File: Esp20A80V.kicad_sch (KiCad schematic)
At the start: 19 parts, among them J1 dcdc, J4 I2C/Uart, Q1 SI2305, SW1 3x button, U1 spi tft with touch (+ sd card), U3 20A 80V dcdc, U4 Wemos S2 Mini

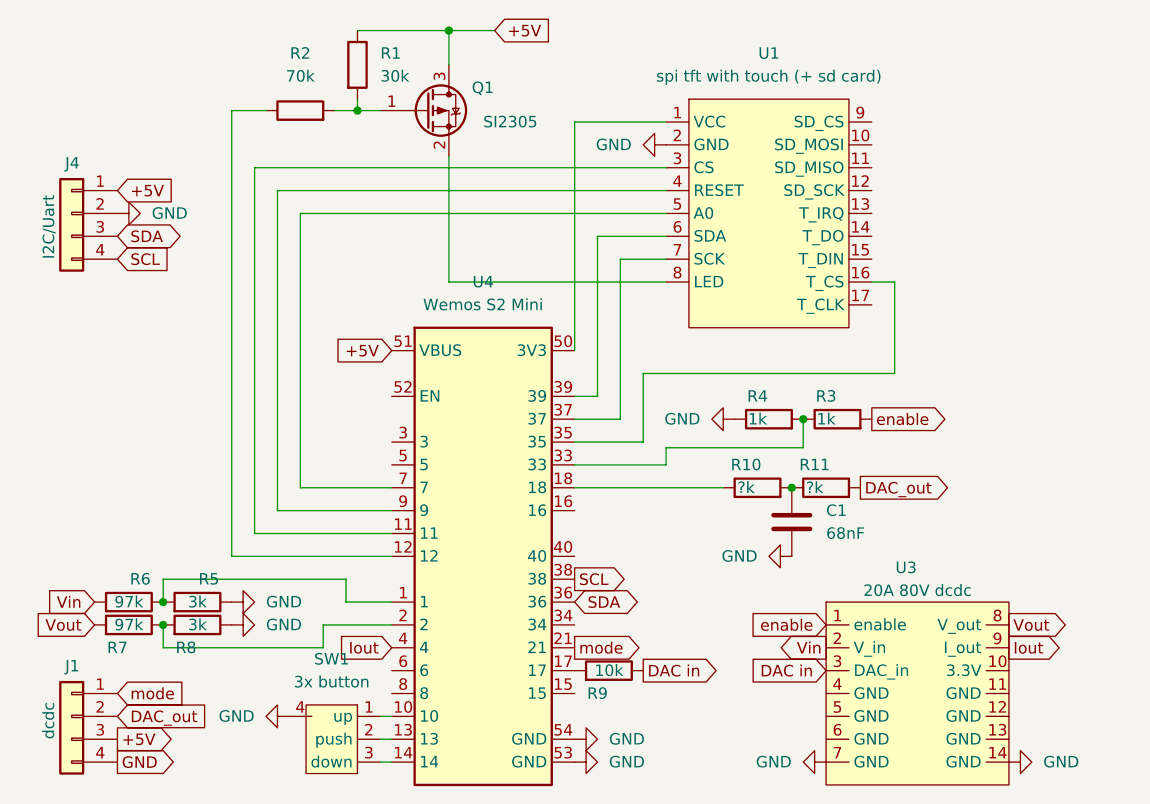
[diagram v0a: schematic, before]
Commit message: footsprints verified and sd card added
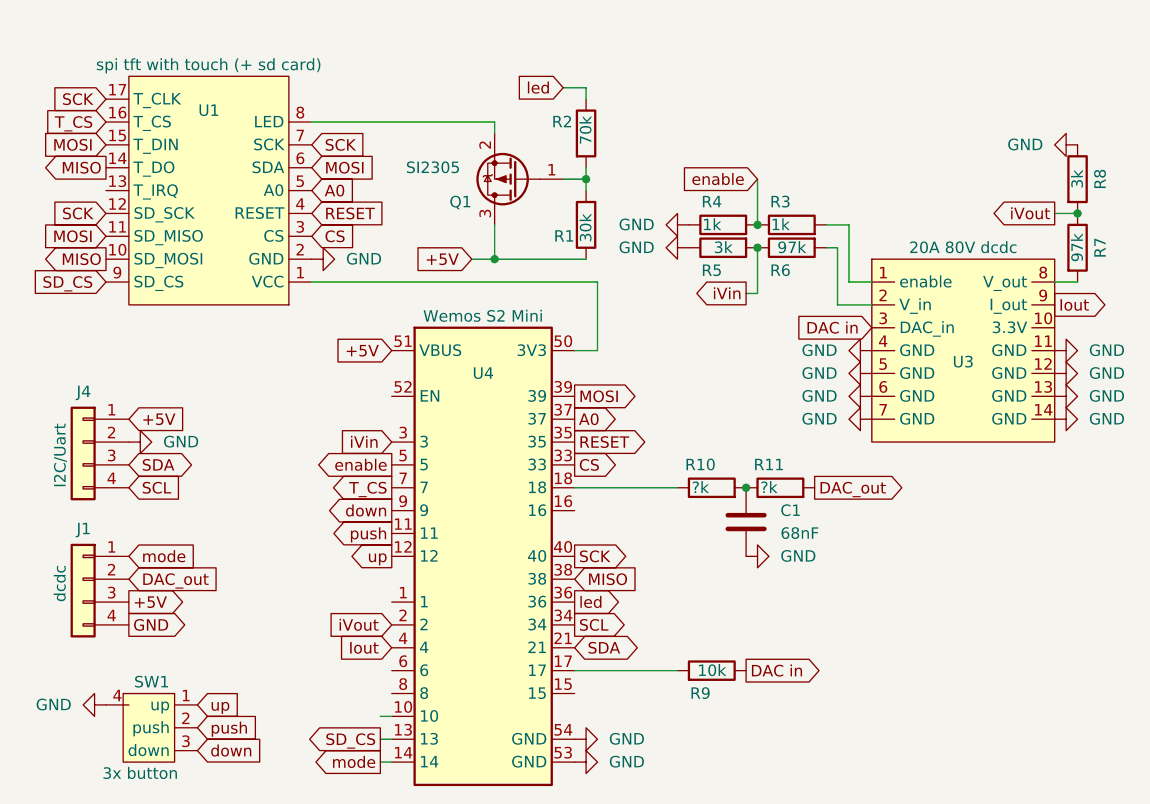
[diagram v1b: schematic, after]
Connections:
- net GND: now also U3.11 (GND), U3.12 (GND), U3.13 (GND), U3.4 (GND), U3.5 (GND), U3.6 (GND)
- net SCL: now also U4.34; no longer U4.38
- net SDA: now also U4.21; no longer U4.36
- net enable: now also R3.1, R4.2, U4.5; no longer R3.2, U3.1 (enable)
- net mode: now also U4.14; no longer U4.21
- net MISO: now reaches U1.10 (SD_MOSI)
- net MISO: now also U1.14 (T_DO), U4.38
- net MOSI: now reaches U1.11 (SD_MISO)
- net MOSI: now also U1.15 (T_DIN), U1.6 (SDA), U4.39
- net SCK: now reaches U1.12 (SD_SCK)
- net SCK: now also U1.17 (T_CLK), U1.7 (SCK), U4.40
- net RESET: now reaches U4.35
- net RESET: now also U1.4 (RESET); no longer U1.16 (T_CS)
- net CS: now reaches U1.3 (CS)
- net CS: now also U4.33; no longer U4.11
- net down: now reaches U4.9
- net down: now also SW1.3 (down); no longer U1.4 (RESET)
- net A0: now reaches U1.5 (A0)
- net A0: now also U4.37; no longer U4.7
- net SD_CS: now reaches U1.9 (SD_CS)
- net SD_CS: now also U4.13
- net iVout: now reaches R7.1, R8.2, U4.2
- net iVin: now reaches R5.2, R6.1
- net iVin: now also U4.3; no longer U4.1
- net at U4.10: no longer SW1.1 (up)
- net push: now reaches SW1.2 (push)
- net push: now also U4.11; no longer U4.13
- net led: now reaches R2.1
- net led: now also U4.36; no longer U4.12
- net Vin: no longer names the net of R6.2, U3.2 (V_in)
- net Vout: no longer names the net of R7.2, U3.8 (V_out)
- new net: R3.2, U3.1 (enable)
- new net T_CS: U1.16 (T_CS), U4.7
- new net up: SW1.1 (up), U4.12
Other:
- moved on the sheet: C1, J1, J4, Q1, R1, R10, R11, R2, R3, R4, R5, R6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

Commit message: jst ph2.0 instead of dupont female
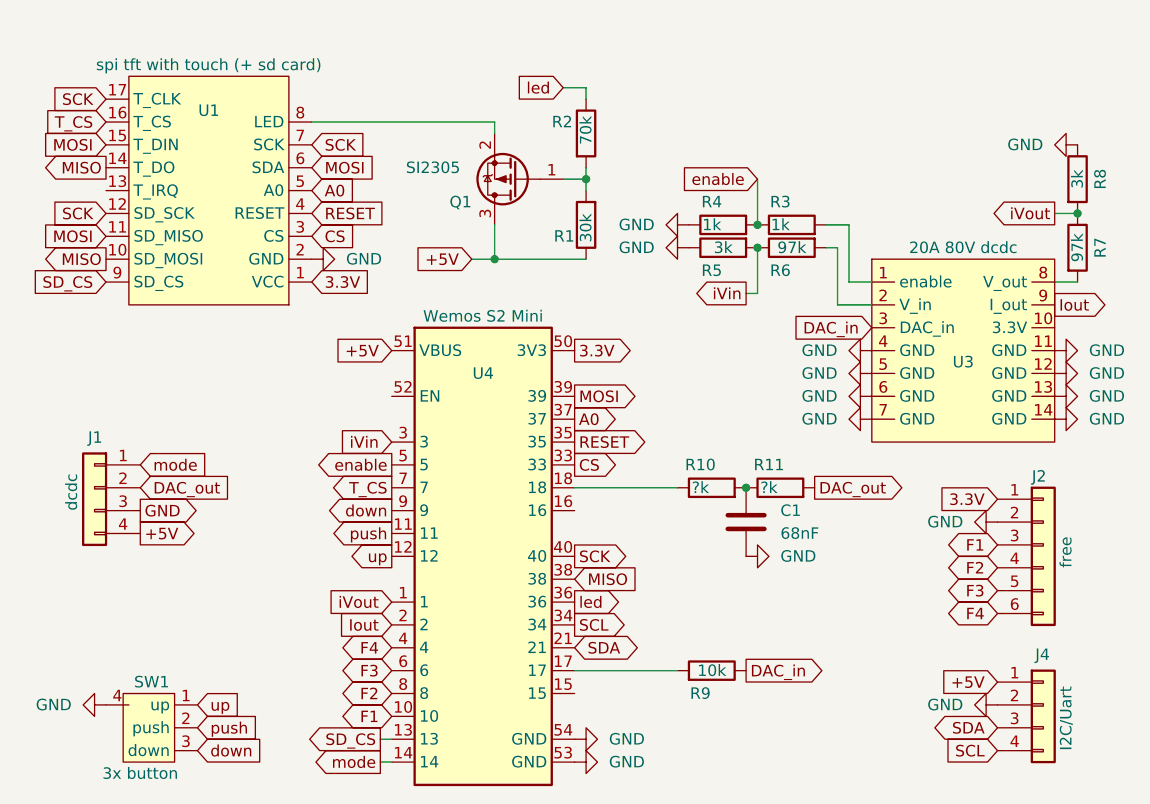
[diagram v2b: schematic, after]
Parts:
- added J2: free, Connector_PinHeader_2.54mm:PinHeader_1x06_P2.54mm_Horizontal, symbol Connector_Generic:Conn_01x06
- J1: footprint Connector_PinHeader_2.54mm:PinHeader_1x04_P2.54mm_Vertical -> Connector_JST:JST_PH_B4B-PH-K_1x04_P2.00mm_Vertical
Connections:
- net +5V: now also J1.4 (Pin_4); no longer J1.3 (Pin_3)
- net GND: now also J1.3 (Pin_3), J2.2 (Pin_2); no longer J1.4 (Pin_4)
- net Iout: now also U4.2; no longer U4.4
- net iVout: now also U4.1; no longer U4.2
- net 3.3V: now reaches U1.1 (VCC), U4.50 (3V3)
- net 3.3V: now also J2.1 (Pin_1)
- net F1: now reaches U4.10
- net F1: now also J2.3 (Pin_3)
- net F3: now reaches U4.6
- net F3: now also J2.5 (Pin_5)
- net F2: now reaches U4.8
- net F2: now also J2.4 (Pin_4)
- net DAC in renamed DAC_in
- new net F4: J2.6 (Pin_6), U4.4
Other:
- moved on the sheet: J1, J4

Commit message: update
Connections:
- net DAC_out: now also J1.1 (Pin_1); no longer J1.2 (Pin_2)
- net mode: now also J1.2 (Pin_2); no longer J1.1 (Pin_1)
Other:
- moved on the sheet: J1, SW1
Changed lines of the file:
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@@
     )
   )
-  (global_label "push" (shape input) (at 107.95 118.11 0) (fields_autoplaced)
-    (effects (font (size 1.27 1.27)) (justify left))
-    (property "Intersheetrefs" "${INTERSHEET_REFS}" (at 115.4103 118.11 0)
+  (global_label "push" (shape input) (at 107.95 96.52 0) (fields_autoplaced)
+    (effects (font (size 1.27 1.27)) (justify left))
+    (property "Intersheetrefs" "${INTERSHEET_REFS}" (at 115.4103 96.52 0)
       (effects (font (size 1.27 1.27)) (justify left) hide)
     )
@@
     )
   )
-  (global_label "up" (shape input) (at 107.95 115.57 0) (fields_autoplaced)
-    (effects (font (size 1.27 1.27)) (justify left))
-    (property "Intersheetrefs" "${INTERSHEET_REFS}" (at 113.2332 115.57 0)
+  (global_label "up" (shape input) (at 107.95 93.98 0) (fields_autoplaced)
+    (effects (font (size 1.27 1.27)) (justify left))
+    (property "Intersheetrefs" "${INTERSHEET_REFS}" (at 113.2332 93.98 0)
       (effects (font (size 1.27 1.27)) (justify left) hide)
     )
@@
     )
   )
-  (global_label "DAC_out" (shape input) (at 101.6 91.44 0) (fields_autoplaced)
-    (effects (font (size 1.27 1.27)) (justify left))
-    (property "Intersheetrefs" "${INTERSHEET_REFS}" (at 112.2051 91.44 0)
-      (effects (font (size 1.27 1.27)) (justify left) hide)
-    )
-  )
-  (global_label "GND" (shape output) (at 101.6 93.98 0) (fields_autoplaced)
-    (effects (font (size 1.27 1.27)) (justify left))
-    (property "Intersheetrefs" "${INTERSHEET_REFS}" (at 108.4557 93.98 0)
+  (global_label "DAC_out" (shape input) (at 97.79 111.76 0) (fields_autoplaced)
+    (effects (font (size 1.27 1.27)) (justify left))
+    (property "Intersheetrefs" "${INTERSHEET_REFS}" (at 108.3951 111.76 0)
+      (effects (font (size 1.27 1.27)) (justify left) hide)
+    )
+  )
+  (global_label "GND" (shape output) (at 97.79 116.84 0) (fields_autoplaced)
+    (effects (font (size 1.27 1.27)) (justify left))
+    (property "Intersheetrefs" "${INTERSHEET_REFS}" (at 104.6457 116.84 0)
       (effects (font (size 1.27 1.27)) (justify left) hide)
     )
@@
     )
   )
-  (global_label "+5V" (shape output) (at 101.6 96.52 0) (fields_autoplaced)
-    (effects (font (size 1.27 1.27)) (justify left))
-    (property "Intersheetrefs" "${INTERSHEET_REFS}" (at 108.4557 96.52 0)
+  (global_label "+5V" (shape output) (at 97.79 119.38 0) (fields_autoplaced)
+    (effects (font (size 1.27 1.27)) (justify left))
+    (property "Intersheetrefs" "${INTERSHEET_REFS}" (at 104.6457 119.38 0)
       (effects (font (size 1.27 1.27)) (justify left) hide)
     )
@@
     )
   )
-  (global_label "down" (shape input) (at 107.95 120.65 0) (fields_autoplaced)
-    (effects (font (size 1.27 1.27)) (justify left))
-    (property "Intersheetrefs" "${INTERSHEET_REFS}" (at 115.7127 120.65 0)
+  (global_label "down" (shape input) (at 107.95 99.06 0) (fields_autoplaced)
+    (effects (font (size 1.27 1.27)) (justify left))
+    (property "Intersheetrefs" "${INTERSHEET_REFS}" (at 115.7127 99.06 0)
       (effects (font (size 1.27 1.27)) (justify left) hide)
     )
@@
     )
   )
-  (global_label "mode" (shape input) (at 101.6 88.9 0) (fields_autoplaced)
-    (effects (font (size 1.27 1.27)) (justify left))
-    (property "Intersheetrefs" "${INTERSHEET_REFS}" (at 109.6651 88.9 0)
+  (global_label "mode" (shape input) (at 97.79 114.3 0) (fields_autoplaced)
+    (effects (font (size 1.27 1.27)) (justify left))
+    (property "Intersheetrefs" "${INTERSHEET_REFS}" (at 105.8551 114.3 0)
       (effects (font (size 1.27 1.27)) (justify left) hide)
     )
@@
     )
   )
-  (symbol (lib_id "Connector_Generic:Conn_01x04") (at 96.52 91.44 0) (mirror y) (unit 1)
-    (in_bom yes) (on_board yes) (dnp no)
-    (property "Reference" "J1" (at 97.409 85.852 0)
-      (effects (font (size 1.27 1.27)) (justify left))
-    )
-    (property "Value" "dcdc" (at 93.98 93.98 90)
-      (effects (font (size 1.27 1.27)) (justify left))
-    )
-    (property "Footprint" "Connector_JST:JST_PH_B4B-PH-K_1x04_P2.00mm_Vertical" (at 93.98 91.44 90)
-      (effects (font (size 1.27 1.27)) hide)
-    )
-    (property "Datasheet" "~" (at 96.52 91.44 0)
+  (symbol (lib_id "Connector_Generic:Conn_01x04") (at 92.71 114.3 0) (mirror y) (unit 1)
+    (in_bom yes) (on_board yes) (dnp no)
+    (property "Reference" "J1" (at 93.599 108.712 0)
+      (effects (font (size 1.27 1.27)) (justify left))
+    )
+    (property "Value" "dcdc" (at 90.17 116.84 90)
+      (effects (font (size 1.27 1.27)) (justify left))
+    )
+    (property "Footprint" "Connector_JST:JST_PH_B4B-PH-K_1x04_P2.00mm_Vertical" (at 90.17 114.3 90)
+      (effects (font (size 1.27 1.27)) hide)
+    )
+    (property "Datasheet" "~" (at 92.71 114.3 0)
       (effects (font (size 1.27 1.27)) hide)
     )
@@
     )
   )
-  (symbol (lib_id "Esp20A80V:3way_dial_switch") (at 105.41 120.65 0) (mirror y) (unit 1)
-    (in_bom yes) (on_board yes) (dnp no)
-    (property "Reference" "SW1" (at 102.87 113.03 0)
-      (effects (font (size 1.27 1.27)))
-    )
-    (property "Value" "3x button" (at 101.6 123.19 0)
-      (effects (font (size 1.27 1.27)))
-    )
-    (property "Footprint" "Esp20A80V:3way dial switch" (at 102.87 125.095 0)
-      (effects (font (size 1.27 1.27)) hide)
-    )
-    (property "Datasheet" "" (at 107.95 118.11 90)
+  (symbol (lib_id "Esp20A80V:3way_dial_switch") (at 105.41 99.06 0) (mirror y) (unit 1)
+    (in_bom yes) (on_board yes) (dnp no)
+    (property "Reference" "SW1" (at 102.87 91.44 0)
+      (effects (font (size 1.27 1.27)))
+    )
+    (property "Value" "3x button" (at 101.6 101.6 0)
+      (effects (font (size 1.27 1.27)))
+    )
+    (property "Footprint" "Esp20A80V:3way dial switch" (at 102.87 103.505 0)
+      (effects (font (size 1.27 1.27)) hide)
+    )
+    (property "Datasheet" "" (at 107.95 96.52 90)
       (effects (font (size 1.27 1.27)) hide)
     )
@@
     )
   )
-  (symbol (lib_id "power:GND") (at 97.79 115.57 270) (unit 1)
+  (symbol (lib_id "power:GND") (at 97.79 93.98 270) (unit 1)
     (in_bom yes) (on_board yes) (dnp no) (fields_autoplaced)
-    (property "Reference" "#PWR01" (at 91.44 115.57 0)
-      (effects (font (size 1.27 1.27)) hide)
-    )
-    (property "Value" "GND" (at 93.98 115.57 90)
-      (effects (font (size 1.27 1.27)) (justify right))
-    )
-    (property "Footprint" "" (at 97.79 115.57 0)
-      (effects (font (size 1.27 1.27)) hide)
-    )
-    (property "Datasheet" "" (at 97.79 115.57 0)
-      (effects (font (size 1.27 1.27)) hide)
-    )
+    (property "Reference" "#PWR01" (at 91.44 93.98 0)
+      (effects (font (size 1.27 1.27)) hide)
+    )
+    (property "Value" "GND" (at 93.98 93.98 90)
+      (effects (font (size 1.27 1.27)) (justify right))
+    )
+    (property "Footprint" "" (at 97.79 93.98 0)
+      (effects (font (size 1.27 1.27)) hide)
+    )
+    (property "Datasheet" "" (at 97.79 93.98 0)
+      (effects (font (size 1.27 1.27)) hide)
+    )

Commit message: update
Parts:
- added R12: 99k, Resistor_SMD:R_0805_2012Metric_Pad1.20x1.40mm_HandSolder, symbol Device:R
- added R13: 1k, Resistor_SMD:R_0805_2012Metric_Pad1.20x1.40mm_HandSolder, symbol Device:R
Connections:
- net 3.3V: now also R12.2
- net Iout: now also R12.1, R13.2; no longer U3.9 (I_out)
- new net: R13.1, U3.9 (I_out)
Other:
- moved on the sheet: R3, R4, R5, R6, R7, R8, U3

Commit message: update
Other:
- moved on the sheet: J1, J2, J4

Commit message: update
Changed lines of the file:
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@@
   (junction (at 191.77 60.96) (diameter 0) (color 0 0 0 0)
   )
-  (junction (at 153.67 119.38) (diameter 0) (color 0 0 0 0)
-  )
   (junction (at 167.64 58.42) (diameter 0) (color 0 0 0 0)
   )
@@
     (stroke (width 0) (type default))
   )
+  (wire (pts (xy 154.94 121.92) (xy 149.86 121.92))
+    (stroke (width 0) (type default))
+  )
   (wire (pts (xy 165.1 71.12) (xy 168.91 71.12))
     (stroke (width 0) (type default))
@@
     (stroke (width 0) (type default))
   )
+  (wire (pts (xy 154.94 119.38) (xy 149.86 119.38))
+    (stroke (width 0) (type default))
+  )
   (wire (pts (xy 167.64 68.58) (xy 168.91 68.58))
     (stroke (width 0) (type default))
@@
     (stroke (width 0) (type default))
   )
-  (wire (pts (xy 149.86 119.38) (xy 153.67 119.38))
-    (stroke (width 0) (type default))
-  )
   (wire (pts (xy 172.72 58.42) (xy 167.64 58.42))
     (stroke (width 0) (type default))
   )
+  (wire (pts (xy 191.77 50.8) (xy 191.77 53.34))
+    (stroke (width 0) (type default))
+  )
   (wire (pts (xy 149.86 91.44) (xy 161.29 91.44))
     (stroke (width 0) (type default))
@@
     (stroke (width 0) (type default))
   )
-  (wire (pts (xy 153.67 119.38) (xy 154.94 119.38))
-    (stroke (width 0) (type default))
-  )
   (wire (pts (xy 120.65 50.8) (xy 140.97 50.8))
     (stroke (width 0) (type default))
@@
     )
   )
-  (netclass_flag "" (length 2.54) (shape round) (at 153.67 119.38 0) (fields_autoplaced)
+  (netclass_flag "" (length 2.54) (shape round) (at 151.13 119.38 0) (fields_autoplaced)
     (effects (font (size 1.27 1.27)) (justify left bottom))
-    (property "Netclass" "ground" (at 154.3685 116.84 0)
+    (property "Netclass" "Ground" (at 151.8285 116.84 0)
       (effects (font (size 1.27 1.27) italic) (justify left))
     )
@@
   (netclass_flag "" (length 2.54) (shape round) (at 97.79 113.03 180) (fields_autoplaced)
     (effects (font (size 1.27 1.27)) (justify right bottom))
-    (property "Netclass" "Power" (at 98.4885 115.57 0)
+    (property "Netclass" "5V" (at 98.4885 115.57 0)
+      (effects (font (size 1.27 1.27) italic) (justify left))
+    )
+  )
+  (netclass_flag "" (length 2.54) (shape round) (at 224.79 78.74 0) (fields_autoplaced)
+    (effects (font (size 1.27 1.27)) (justify left bottom))
+  )
+  (netclass_flag "" (length 2.54) (shape round) (at 149.86 76.2 0) (fields_autoplaced)
+    (effects (font (size 1.27 1.27)) (justify left bottom))
+    (property "Netclass" "3.3V" (at 150.5585 73.66 0)
+      (effects (font (size 1.27 1.27) italic) (justify left))
+    )
+  )
+  (netclass_flag "" (length 2.54) (shape round) (at 130.81 50.8 0) (fields_autoplaced)
+    (effects (font (size 1.27 1.27)) (justify left bottom))
+    (property "Netclass" "led" (at 131.5085 48.26 0)
       (effects (font (size 1.27 1.27) italic) (justify left))
     )
@@
     )
   )
-  (symbol (lib_id "power:GND") (at 149.86 121.92 90) (unit 1)
+  (symbol (lib_id "power:GND") (at 154.94 121.92 90) (unit 1)
     (in_bom yes) (on_board yes) (dnp no) (fields_autoplaced)
-    (property "Reference" "#PWR04" (at 156.21 121.92 0)
-      (effects (font (size 1.27 1.27)) hide)
-    )
-    (property "Value" "GND" (at 153.67 121.92 90)
-      (effects (font (size 1.27 1.27)) (justify right))
-    )
-    (property "Footprint" "" (at 149.86 121.92 0)
-      (effects (font (size 1.27 1.27)) hide)
-    )
-    (property "Datasheet" "" (at 149.86 121.92 0)
+    (property "Reference" "#PWR04" (at 161.29 121.92 0)
+      (effects (font (size 1.27 1.27)) hide)
+    )
+    (property "Value" "GND" (at 158.75 121.92 90)
+      (effects (font (size 1.27 1.27)) (justify right))
+    )
+    (property "Footprint" "" (at 154.94 121.92 0)
+      (effects (font (size 1.27 1.27)) hide)
+    )
+    (property "Datasheet" "" (at 154.94 121.92 0)
       (effects (font (size 1.27 1.27)) hide)
     )
@@
     )
   )
-  (symbol (lib_id "power:GND") (at 153.67 119.38 90) (unit 1)
+  (symbol (lib_id "power:GND") (at 154.94 119.38 90) (unit 1)
     (in_bom yes) (on_board yes) (dnp no) (fields_autoplaced)
-    (property "Reference" "#PWR05" (at 160.02 119.38 0)
-      (effects (font (size 1.27 1.27)) hide)
-    )
-    (property "Value" "GND" (at 157.48 119.38 90)
-      (effects (font (size 1.27 1.27)) (justify right))
-    )
-    (property "Footprint" "" (at 153.67 119.38 0)
-      (effects (font (size 1.27 1.27)) hide)
-    )
-    (property "Datasheet" "" (at 153.67 119.38 0)
+    (property "Reference" "#PWR05" (at 161.29 119.38 0)
+      (effects (font (size 1.27 1.27)) hide)
+    )
+    (property "Value" "GND" (at 158.75 119.38 90)
+      (effects (font (size 1.27 1.27)) (justify right))
+    )
+    (property "Footprint" "" (at 154.94 119.38 0)
+      (effects (font (size 1.27 1.27)) hide)
+    )
+    (property "Datasheet" "" (at 154.94 119.38 0)
       (effects (font (size 1.27 1.27)) hide)
     )
@@
     )
   )
-  (symbol (lib_id "power:GND") (at 191.77 53.34 270) (mirror x) (unit 1)
-    (in_bom yes) (on_board yes) (dnp no)
-    (property "Reference" "#PWR09" (at 185.42 53.34 0)
-      (effects (font (size 1.27 1.27)) hide)
-    )
-    (property "Value" "GND" (at 187.96 53.34 90)
-      (effects (font (size 1.27 1.27)) (justify right))
-    )
-    (property "Footprint" "" (at 191.77 53.34 0)
-      (effects (font (size 1.27 1.27)) hide)
-    )
-    (property "Datasheet" "" (at 191.77 53.34 0)
-      (effects (font (size 1.27 1.27)) hide)
-    )
+  (symbol (lib_id "power:GND") (at 191.77 50.8 270) (mirror x) (unit 1)
+    (in_bom yes) (on_board yes) (dnp no)
+    (property "Reference" "#PWR09" (at 185.42 50.8 0)
+      (effects (font (size 1.27 1.27)) hide)
+    )
+    (property "Value" "GND" (at 187.96 50.8 90)
+      (effects (font (size 1.27 1.27)) (justify right))
+    )
+    (property "Footprint" "" (at 191.77 50.8 0)
+      (effects (font (size 1.27 1.27)) hide)
+    )
+    (property "Datasheet" "" (at 191.77 50.8 0)
+      (effects (font (size 1.27 1.27)) hide)
+    )
